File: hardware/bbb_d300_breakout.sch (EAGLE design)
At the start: 10 parts, among them SW1 JTP1236, X1 STEPCRAFT, X2 RJ45, X3 RJ45

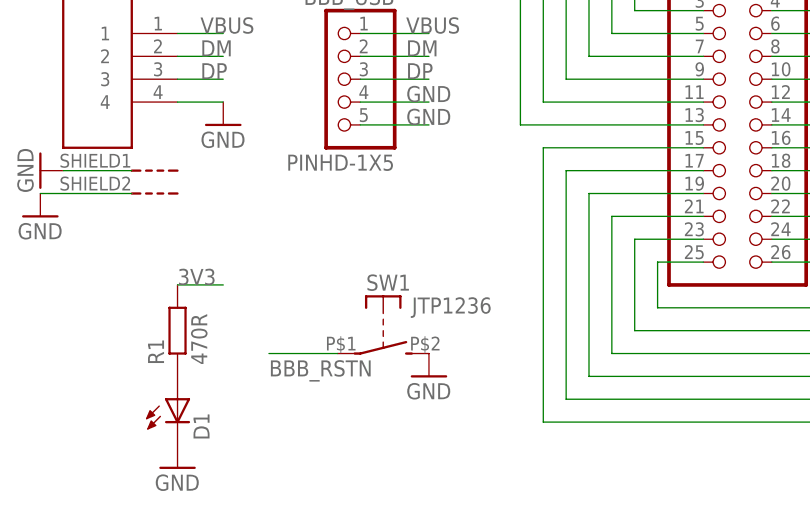
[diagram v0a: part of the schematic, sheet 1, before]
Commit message: swap USB and ETH position
Signed-off-by: Vladimir Pantelic <vladimir@pantelic.net>
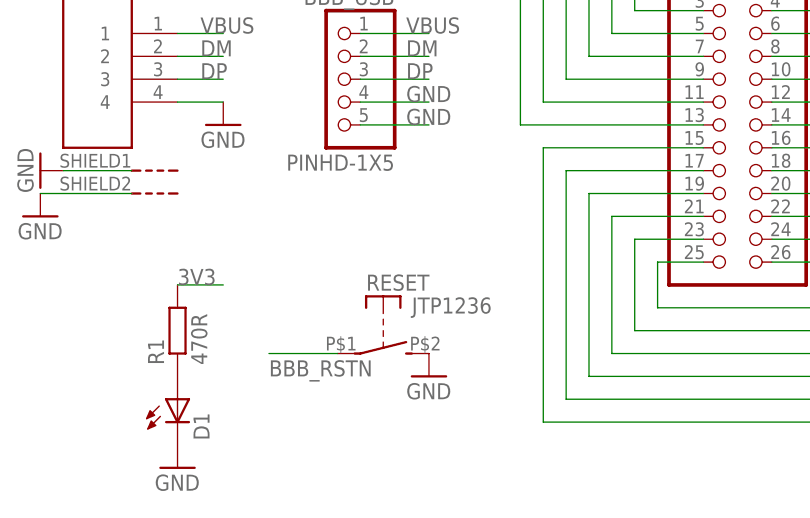
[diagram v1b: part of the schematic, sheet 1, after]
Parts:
- renumbered SW1 to RESET
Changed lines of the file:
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@@
 <part name="U$2" library="!frames" deviceset="DINA4_L_DOCSMAL" device=""/>
 <part name="BBB_USB" library="00vp" deviceset="PINHD-1X5" device=""/>
-<part name="SW1" library="00nikis" deviceset="JTP1236" device=""/>
+<part name="RESET" library="00nikis" deviceset="JTP1236" device=""/>
 <part name="BBB" library="pinhead" deviceset="PINHD-2X13" device=""/>
 <part name="X2" library="00vp" deviceset="RJ45" device=""/>
@@
 </instance>
 <instance part="BBB_USB" gate="G$1" x="58.42" y="38.1" rot="MR0"/>
-<instance part="SW1" gate="G$1" x="63.5" y="7.62" rot="R270"/>
+<instance part="RESET" gate="G$1" x="63.5" y="7.62" rot="R270"/>
 <instance part="BBB" gate="A" x="101.6" y="33.02"/>
 <instance part="X2" gate="G$1" x="30.48" y="83.82" rot="MR0"/>
@@
 </segment>
 <segment>
-<pinref part="SW1" gate="G$1" pin="S"/>
+<pinref part="RESET" gate="G$1" pin="S"/>
 <pinref part="GND2" gate="1" pin="GND"/>
 </segment>
@@
 <net name="BBB_RSTN" class="0">
 <segment>
-<pinref part="SW1" gate="G$1" pin="P"/>
+<pinref part="RESET" gate="G$1" pin="P"/>
 <wire x1="58.42" y1="7.62" x2="50.8" y2="7.62" width="0.1524" layer="91"/>
 <label x="50.8" y="5.08" size="1.778" layer="95"/>
